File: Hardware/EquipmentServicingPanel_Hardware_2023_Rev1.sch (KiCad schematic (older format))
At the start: 49 parts

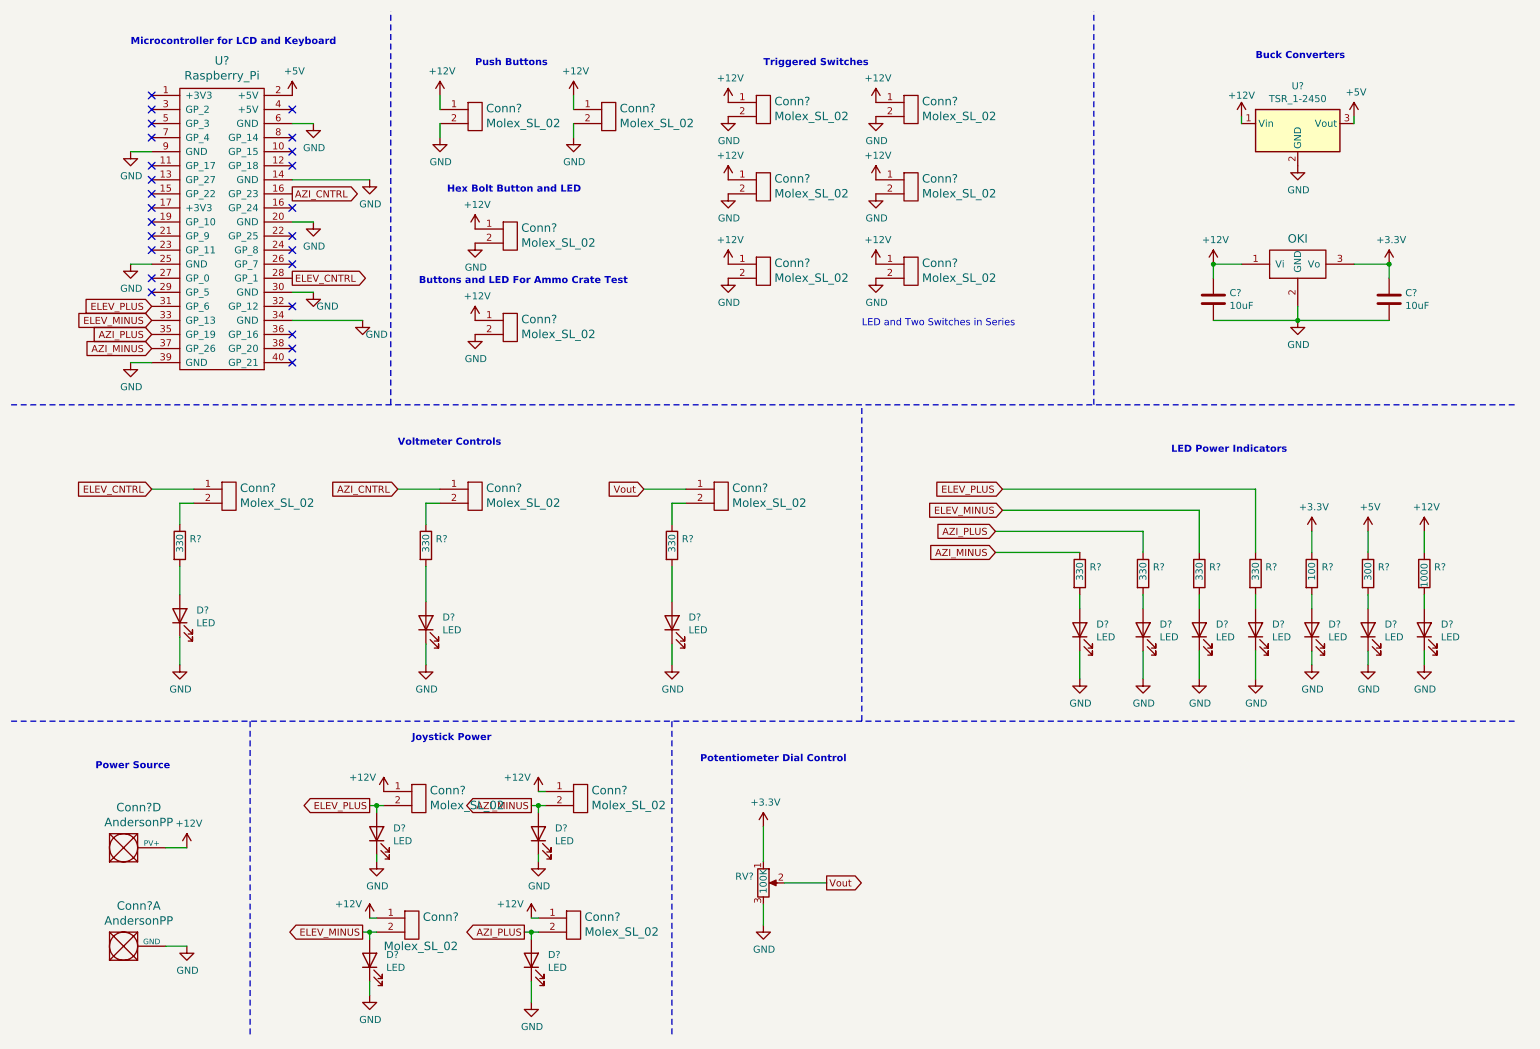
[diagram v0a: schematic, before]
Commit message: Added Vias and removed extra voltmeter
Added vias and removed one of the three voltmeters that used a potentiometer to test the wrist
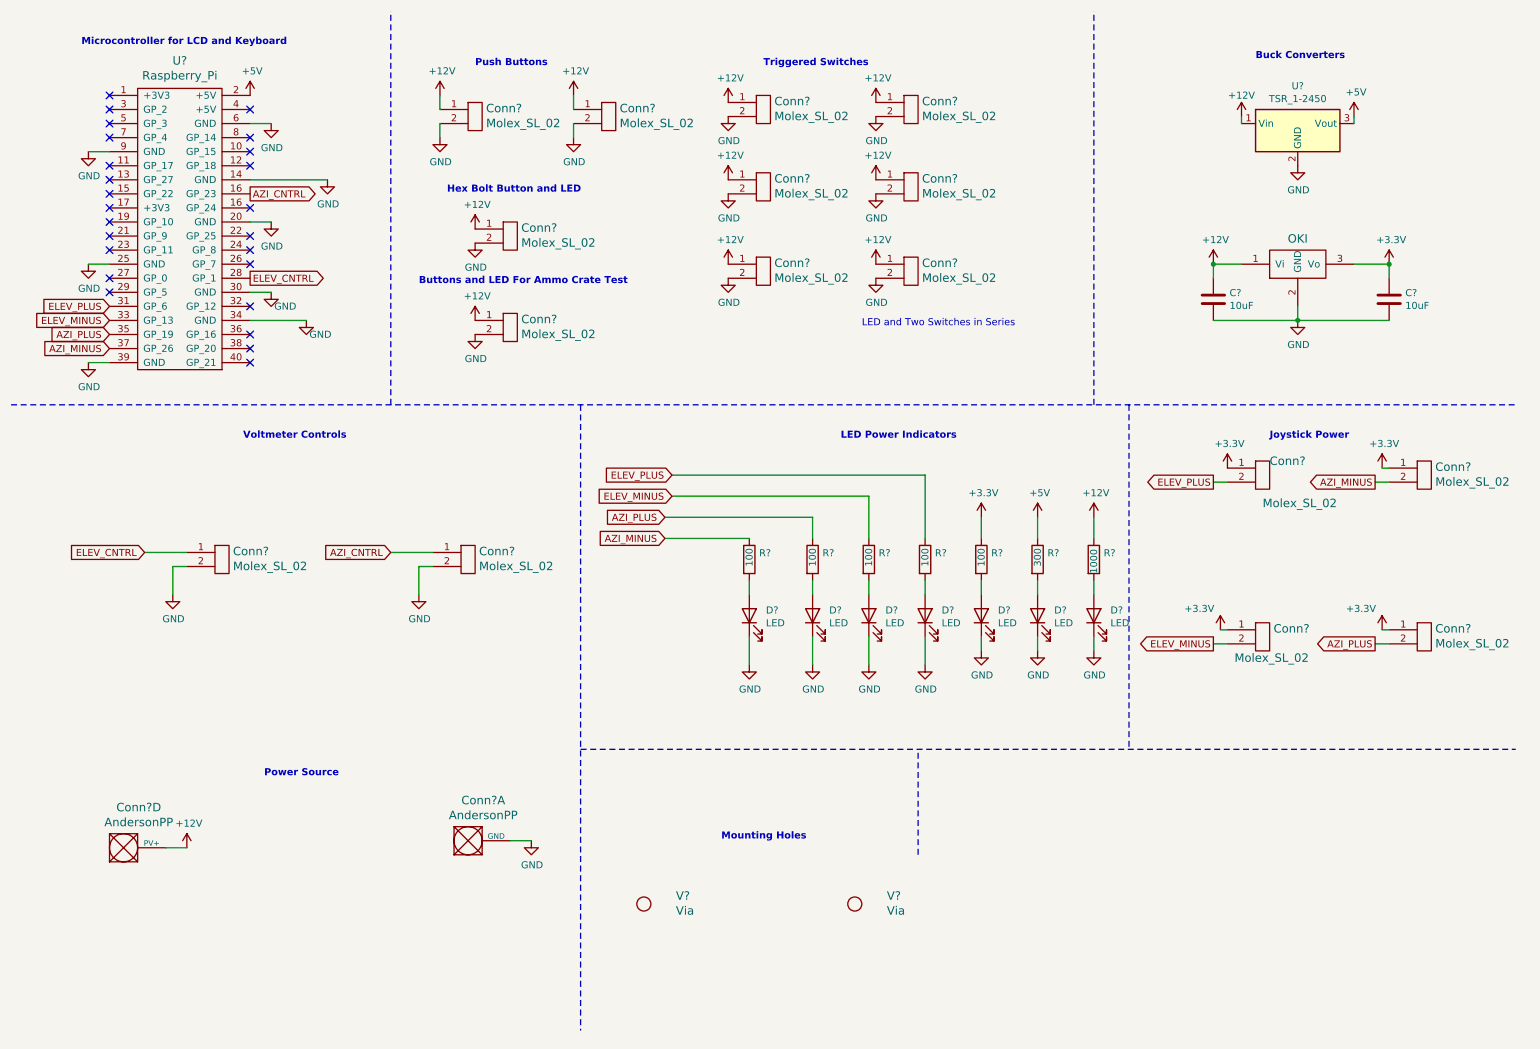
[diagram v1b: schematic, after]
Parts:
- removed Conn?: Molex_SL_02, symbol MRDT_Connectors:Molex_SL_02
- removed D? (x7): LED, symbol Device:LED
- removed R? (x3): 330, symbol Device:R
- removed RV?: 100K, symbol Device:R_POT
- added V? (x2): Via, symbol MRDT_Drill_Holes:Via
- R? (x4): value 330 -> 100
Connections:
- net +12V: no longer Conn?.1, Conn?.1, Conn?.1, Conn?.1
- net +3V3: now also Conn?.1, Conn?.1, Conn?.1, Conn?.1
- net GND: now also Conn?.2, Conn?.2
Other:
- note added: "Mounting Holes"
- note removed: "Potentiometer Dial Control"
- moved on the sheet: Conn?, Conn?A, D?, R?, U?

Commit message: changes were made to fix pin 16 issues
different ports were used on the raspberry pi so no connects could be placed on the duplicated pin 16
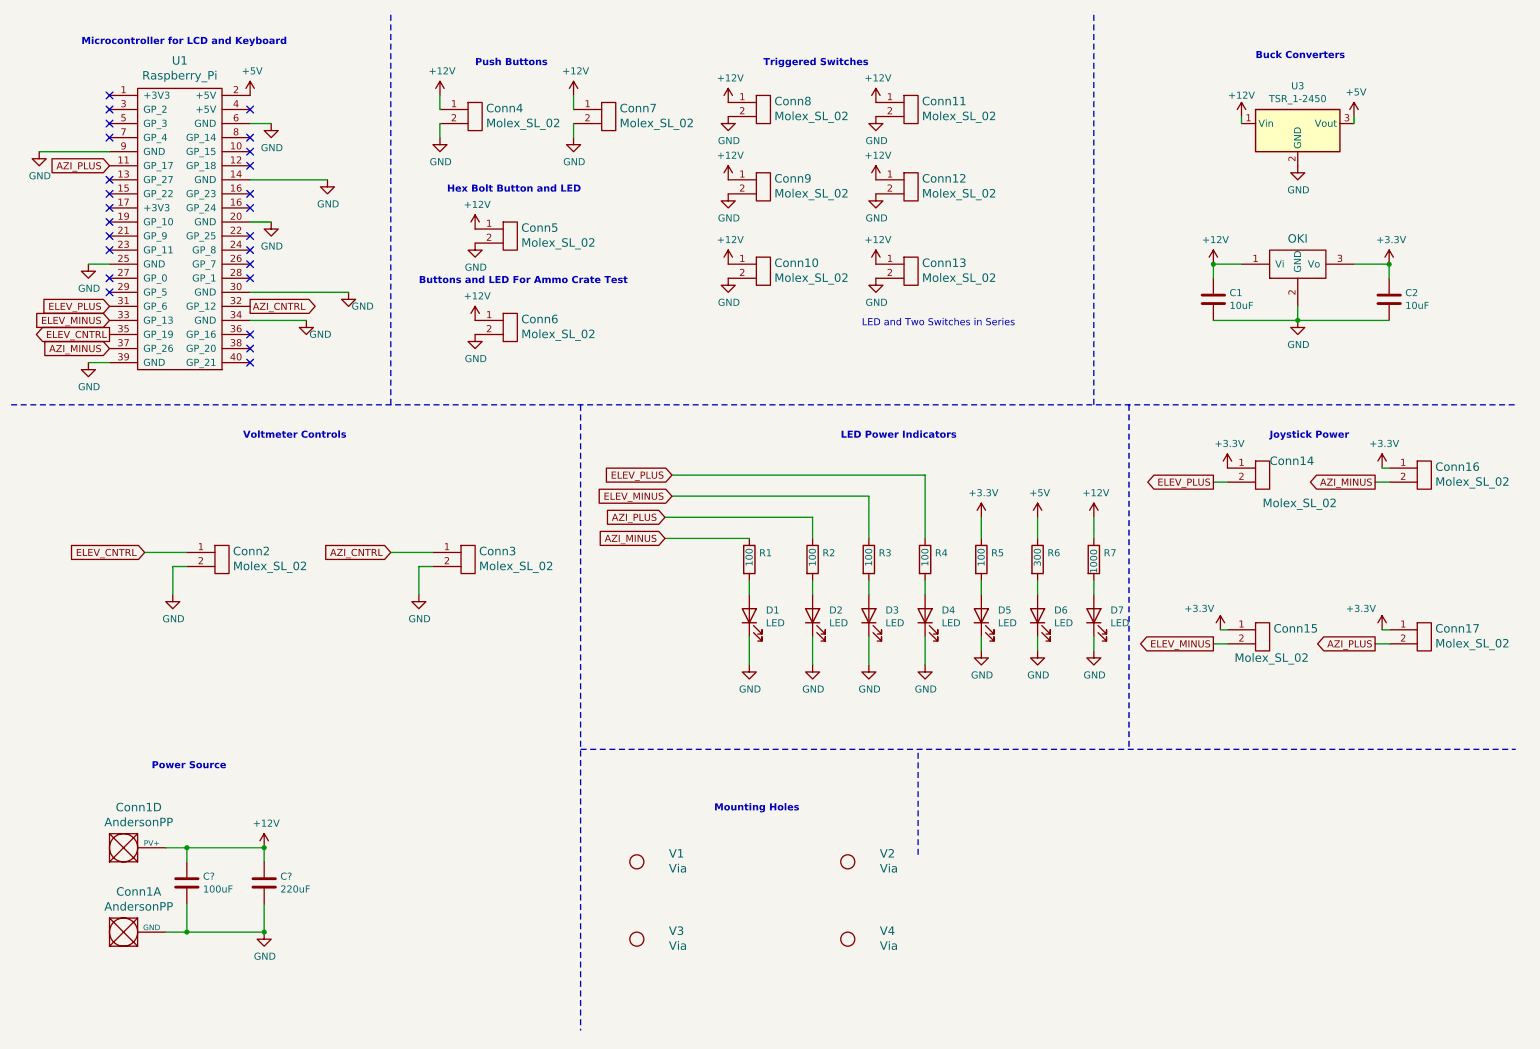
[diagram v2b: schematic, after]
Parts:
- removed U?: Raspberry_Pi, symbol MRDT_Shields:Raspberry_Pi
- added C?: 100uF, symbol Device:C
- added C?: 220uF, symbol Device:C
- added U1: Raspberry_Pi, symbol MRDT_Shields:Raspberry_Pi
- added V3, V4: Via, symbol MRDT_Drill_Holes:Via
- gave numbers to parts that had none: 37
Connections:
- net +12V: now also C?.1, C?.1
- net +5V: now also U1.2 (+5V)
- net AZI_CNTRL: now also U1.32 (GP_12)
- net AZI_MINUS: now also U1.37 (GP_26)
- net AZI_PLUS: now also U1.11 (GP_17)
- net ELEV_CNTRL: now also U1.35 (GP_19)
- net ELEV_MINUS: now also U1.33 (GP_13)
- net ELEV_PLUS: now also U1.31 (GP_6)
- net GND: now also C?.2, C?.2, U1.14 (GND), U1.20 (GND), U1.25 (GND), U1.30 (GND), U1.34 (GND), U1.39 (GND), U1.6 (GND), U1.9 (GND)
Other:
- moved on the sheet: Conn1A, V1, V2

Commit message: Created Layout
Created Layout for PCB design of Equipment Servicing Panel
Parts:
- C1, C2: footprint (none) -> Capacitor_SMD:C_0201_0603Metric_Pad0.64x0.40mm_HandSolder
- C3, C4: renamed from C?; footprint (none) -> Capacitor_THT:CP_Radial_D6.3mm_P2.50mm
- Conn1: footprint (none) -> MRDT_Connectors:Square_Anderson_2_H_Stacked
- Conn10, Conn11, Conn12, Conn13, Conn14, Conn15, Conn16, Conn17, Conn2, Conn3, Conn4, Conn5, Conn6, Conn7, Conn8, Conn9: footprint (none) -> MRDT_Connectors:MOLEX_SL_02_Horizontal
- D1, D2, D3, D4, D5, D6, D7: footprint (none) -> LED_SMD:LED_0201_0603Metric_Pad0.64x0.40mm_HandSolder
- R1, R2, R3, R4, R5, R6, R7: footprint (none) -> Resistor_SMD:R_0603_1608Metric_Pad0.98x0.95mm_HandSolder
- U1: footprint (none) -> MRDT_Shields:RASPBERRY_PI_HEADERS
- U2: footprint (none) -> MRDT_Devices:OKI_Horizontal
- U3: footprint Converter_DCDC:Converter_DCDC_TRACO_TSR-1_THT -> MRDT_Devices:TSR_1-2433
- V1, V2, V3, V4: footprint (none) -> MRDT_Drill_Holes:4_40_Hole_Corner
